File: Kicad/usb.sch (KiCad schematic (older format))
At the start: 28 parts, among them J1001 USB Ports External, J1002 USB Ports Internal, U1001 AP2501, U1002 MIC2005A-2YM5, U1003 MIC2005A-2YM5, U1004 XR22404CG28, U1005 MIC2005A-2YM5, U1006 MIC2005A-2YM5, Y1001 12M

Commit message: Switch some of the radial THT Electrolytic caps for SMD MLCCs.
Also changed the STM32 for an LQFP-32 as it has a bigger pitch on the
pins.

The LQFP is easier to solder than the TSSOP, and the MLCC takes are
cheaper and take up less space.
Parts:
- C1003, C1005: value 4u7 -> 4u7 10V; footprint Capacitor_THT:CP_Radial_D6.3mm_P2.50mm -> Capacitor_SMD:C_0805_2012Metric_Pad1.15x1.40mm_HandSolder; symbol Device:CP -> Device:C; Digikey 493-12612-1-ND -> 1276-6464-1-ND; MPN UVK2A4R7MDD1TD -> CL21A475KPFNNNG; Manufacturer Nichicon -> Samsung
- C1006, C1007, C1010, C1011: value 120u -> 120u 16V; Digikey 493-17035-ND -> 493-1520-ND; MPN UPJ1H121MPD -> UHE1C121MED
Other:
- moved on the sheet: C1002, C1004, R1004, R1005, R1006

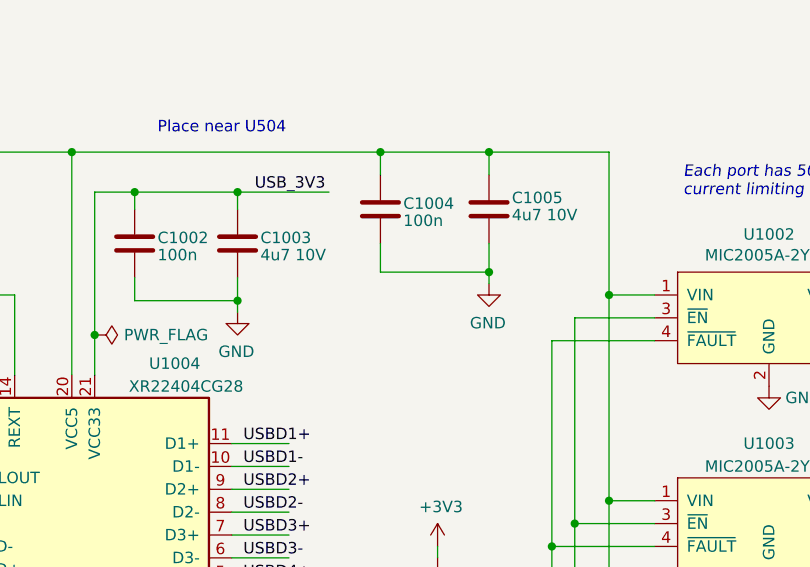
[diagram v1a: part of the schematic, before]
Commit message: Update 4u7 cap to 16V
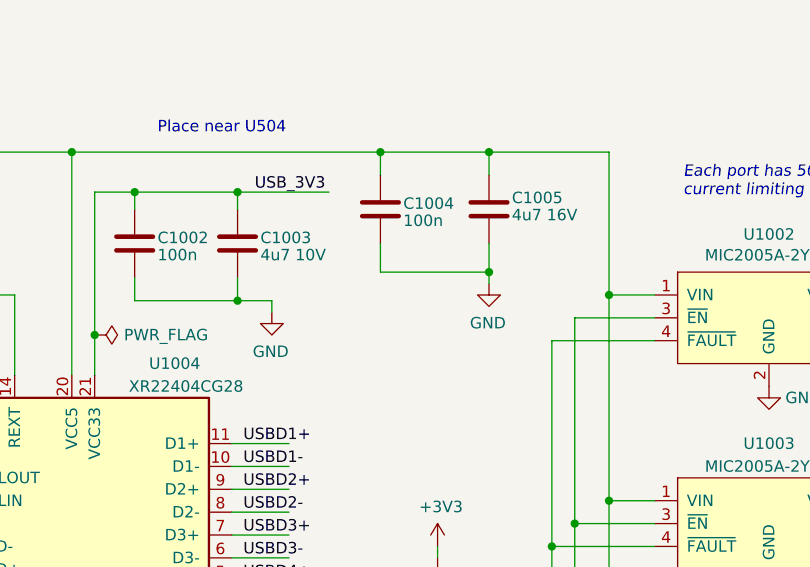
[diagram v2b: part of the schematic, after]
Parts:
- C1005: value 4u7 10V -> 4u7 16V; Digikey 1276-6464-1-ND -> 1276-1065-1-ND; MPN CL21A475KPFNNNG -> CL21A475KOFNNNE
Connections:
- wire segments 151 -> 152
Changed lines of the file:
@@
 P 6500 1750
 F 0 "C1005" H 6600 1800 50  0000 L CNN
-F 1 "4u7 10V" H 6600 1725 50  0000 L CNN
+F 1 "4u7 16V" H 6600 1725 50  0000 L CNN
 F 2 "Capacitor_SMD:C_0805_2012Metric_Pad1.15x1.40mm_HandSolder" H 6538 1600 50  0001 C CNN
 F 3 "~" H 6500 1750 50  0001 C CNN
 F 4 "0" H 6500 1750 50  0001 C CNN "DNP"
-F 5 "1276-6464-1-ND" H 6500 1750 50  0001 C CNN "Digikey"
-F 6 "CL21A475KPFNNNG" H 6500 1750 50  0001 C CNN "MPN"
+F 5 "1276-1065-1-ND" H 6500 1750 50  0001 C CNN "Digikey"
+F 6 "CL21A475KOFNNNE" H 6500 1750 50  0001 C CNN "MPN"
 F 7 "Samsung" H 6500 1750 50  0001 C CNN "Manufacturer"
 	1    6500 1750
@@
 L power:GND #PWR01022
 U 1 1 60555863
-P 5400 2200
-F 0 "#PWR01022" H 5400 1950 50  0001 C CNN
-F 1 "GND" H 5405 2027 50  0000 C CNN
-F 2 "" H 5400 2200 50  0001 C CNN
-F 3 "" H 5400 2200 50  0001 C CNN
-	1    5400 2200
-	-1   0    0    -1
-$EndComp
-Wire Wire Line
-	5400 2200 5400 2150
-Connection ~ 5400 2150
+P 5550 2200
+F 0 "#PWR01022" H 5550 1950 50  0001 C CNN
+F 1 "GND" H 5555 2027 50  0000 C CNN
+F 2 "" H 5550 2200 50  0001 C CNN
+F 3 "" H 5550 2200 50  0001 C CNN
+	1    5550 2200
+	-1   0    0    -1
+$EndComp
 Connection ~ 6025 1500
 Connection ~ 6500 1500
@@
 Wire Wire Line
 	6025 1500 6500 1500
+Wire Wire Line
+	5400 2150 5550 2150
+Wire Wire Line
+	5550 2150 5550 2200
+Connection ~ 5400 2150
 $EndSCHEMATC

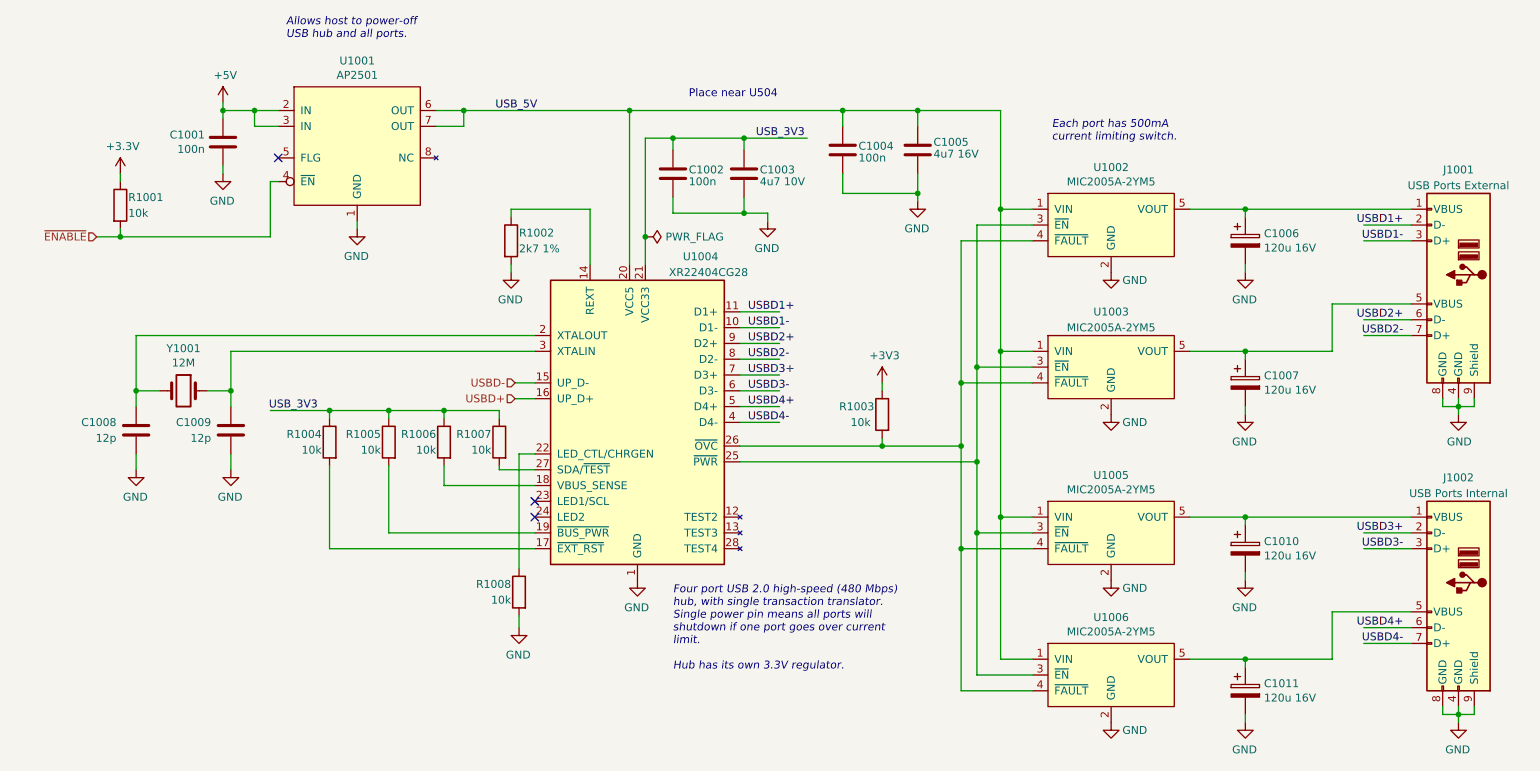
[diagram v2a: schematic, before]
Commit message: Added 12-bit video DAC.
Also had to change footprints to suit Kicad 5.1.9
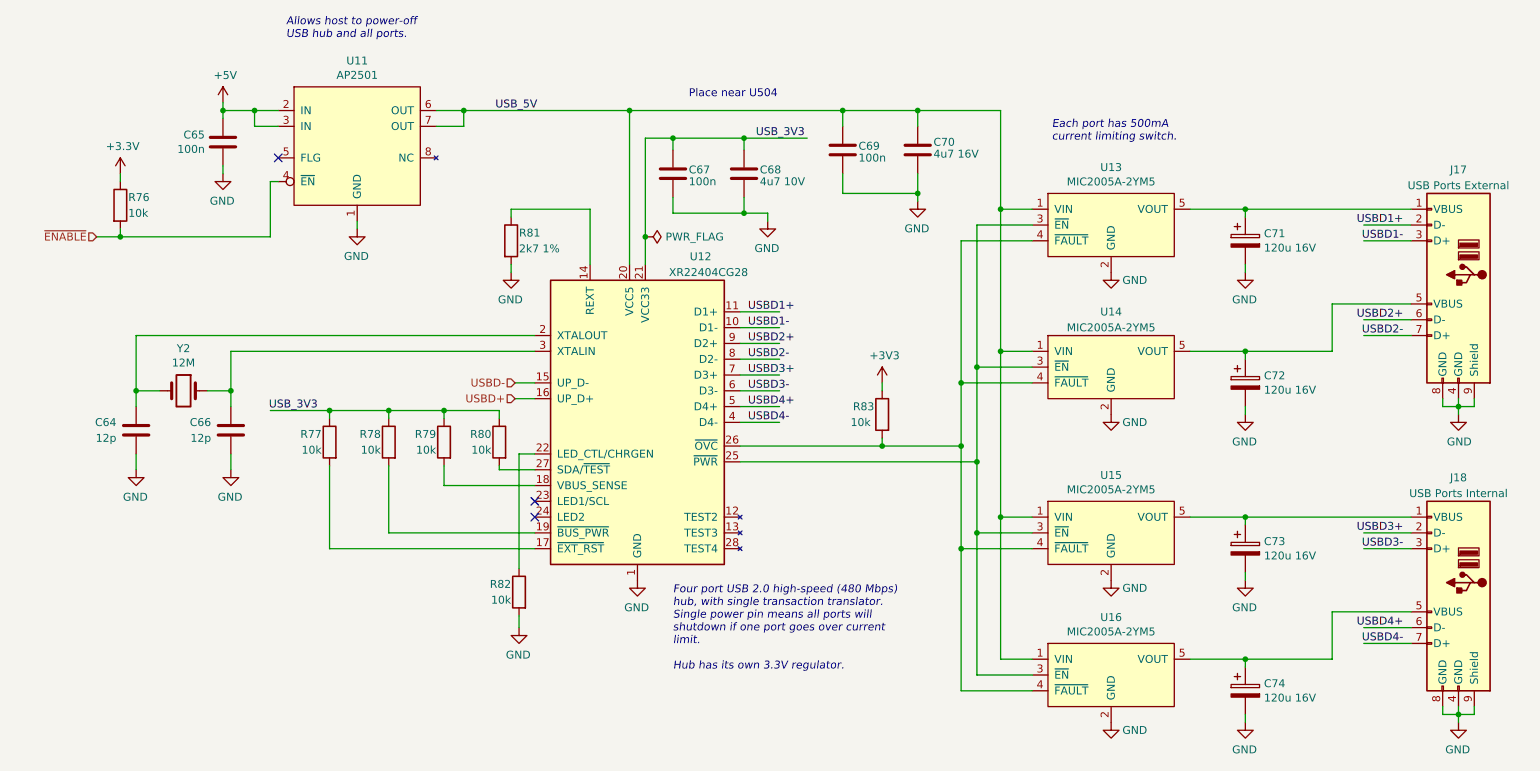
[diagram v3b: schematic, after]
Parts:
- C64: renamed from C1008; footprint Capacitor_SMD:C_0805_2012Metric_Pad1.15x1.40mm_HandSolder -> Capacitor_SMD:C_0805_2012Metric_Pad1.18x1.45mm_HandSolder
- C65: renamed from C1001; footprint Capacitor_SMD:C_0805_2012Metric_Pad1.15x1.40mm_HandSolder -> Capacitor_SMD:C_0805_2012Metric_Pad1.18x1.45mm_HandSolder
- C66: renamed from C1009; footprint Capacitor_SMD:C_0805_2012Metric_Pad1.15x1.40mm_HandSolder -> Capacitor_SMD:C_0805_2012Metric_Pad1.18x1.45mm_HandSolder
- C67: renamed from C1002; footprint Capacitor_SMD:C_0805_2012Metric_Pad1.15x1.40mm_HandSolder -> Capacitor_SMD:C_0805_2012Metric_Pad1.18x1.45mm_HandSolder
- C68: renamed from C1003; footprint Capacitor_SMD:C_0805_2012Metric_Pad1.15x1.40mm_HandSolder -> Capacitor_SMD:C_0805_2012Metric_Pad1.18x1.45mm_HandSolder
- C69: renamed from C1004; footprint Capacitor_SMD:C_0805_2012Metric_Pad1.15x1.40mm_HandSolder -> Capacitor_SMD:C_0805_2012Metric_Pad1.18x1.45mm_HandSolder
- C70: renamed from C1005; footprint Capacitor_SMD:C_0805_2012Metric_Pad1.15x1.40mm_HandSolder -> Capacitor_SMD:C_0805_2012Metric_Pad1.18x1.45mm_HandSolder
- R76: renamed from R1001; footprint Resistor_SMD:R_0805_2012Metric_Pad1.15x1.40mm_HandSolder -> Resistor_SMD:R_0805_2012Metric_Pad1.20x1.40mm_HandSolder
- R77: renamed from R1004; footprint Resistor_SMD:R_0805_2012Metric_Pad1.15x1.40mm_HandSolder -> Resistor_SMD:R_0805_2012Metric_Pad1.20x1.40mm_HandSolder
- R78: renamed from R1005; footprint Resistor_SMD:R_0805_2012Metric_Pad1.15x1.40mm_HandSolder -> Resistor_SMD:R_0805_2012Metric_Pad1.20x1.40mm_HandSolder
- R79: renamed from R1006; footprint Resistor_SMD:R_0805_2012Metric_Pad1.15x1.40mm_HandSolder -> Resistor_SMD:R_0805_2012Metric_Pad1.20x1.40mm_HandSolder
- R80: renamed from R1007; footprint Resistor_SMD:R_0805_2012Metric_Pad1.15x1.40mm_HandSolder -> Resistor_SMD:R_0805_2012Metric_Pad1.20x1.40mm_HandSolder
- R81: renamed from R1002; footprint Resistor_SMD:R_0805_2012Metric_Pad1.15x1.40mm_HandSolder -> Resistor_SMD:R_0805_2012Metric_Pad1.20x1.40mm_HandSolder
- R82: renamed from R1008; footprint Resistor_SMD:R_0805_2012Metric_Pad1.15x1.40mm_HandSolder -> Resistor_SMD:R_0805_2012Metric_Pad1.20x1.40mm_HandSolder
- R83: renamed from R1003; footprint Resistor_SMD:R_0805_2012Metric_Pad1.15x1.40mm_HandSolder -> Resistor_SMD:R_0805_2012Metric_Pad1.20x1.40mm_HandSolder
- renumbered C1006 to C71, C1007 to C72, C1010 to C73, C1011 to C74, J1001 to J17, J1002 to J18, U1001 to U11, U1004 to U12, U1002 to U13, U1003 to U14, U1005 to U15, U1006 to U16, Y1001 to Y2

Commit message: Add 4-bit Video DAC, and re-wire BMC.
Now the BMC is an SPI device, and has a four-wire UART.
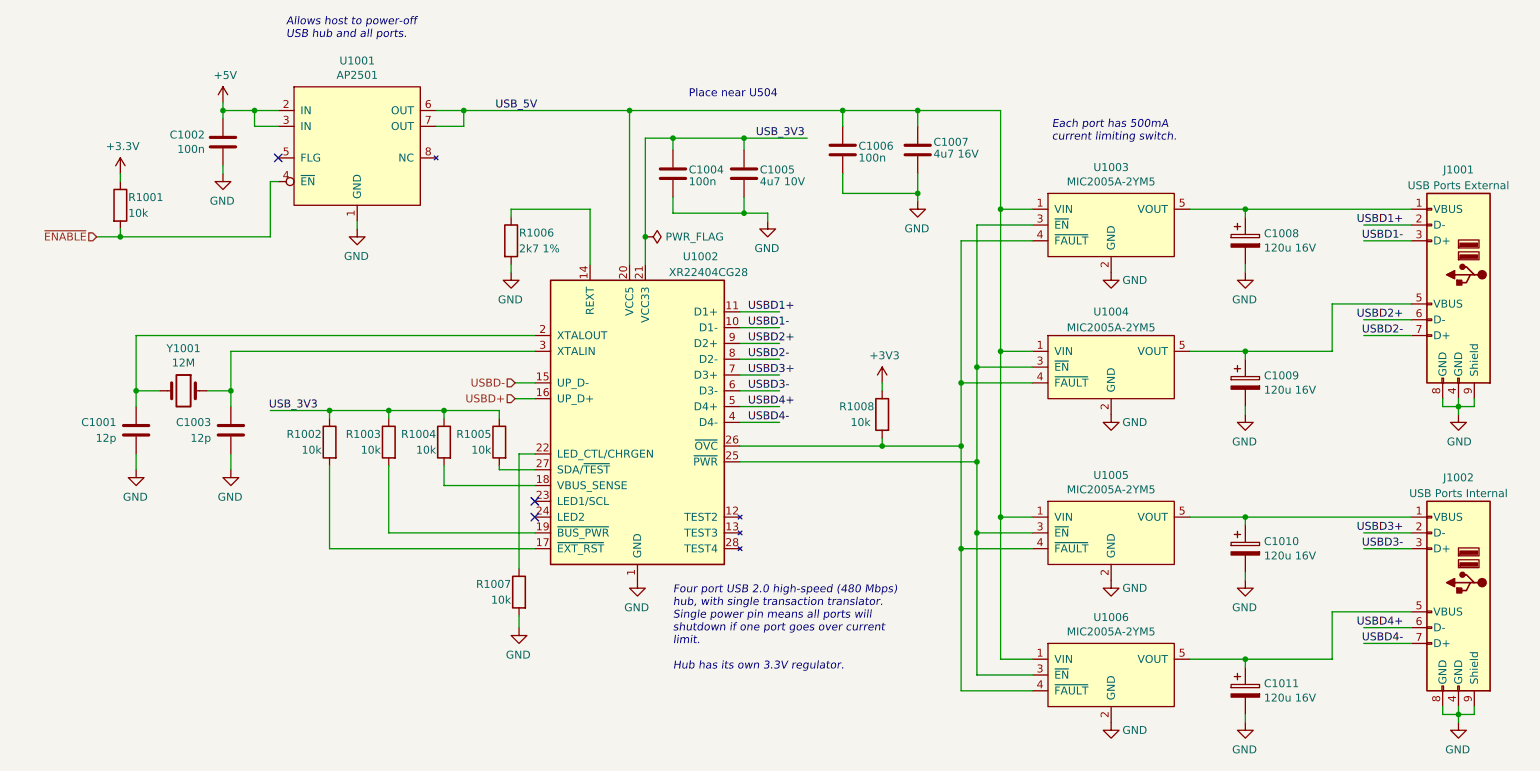
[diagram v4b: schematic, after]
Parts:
- renumbered C64 to C1001, C65 to C1002, C66 to C1003, C67 to C1004, C68 to C1005, C69 to C1006, C70 to C1007, C71 to C1008, C72 to C1009, C73 to C1010, C74 to C1011, J17 to J1001, J18 to J1002, R76 to R1001, R77 to R1002, R78 to R1003, R79 to R1004, R80 to R1005, R81 to R1006, R82 to R1007, R83 to R1008, U11 to U1001, U12 to U1002, U13 to U1003, U14 to U1004, U15 to U1005, U16 to U1006, Y2 to Y1001
